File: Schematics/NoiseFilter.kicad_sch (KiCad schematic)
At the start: 97 parts, among them J68 Conn_01x04, J69 Conn_01x05, Q10 2N3906, Q11 2N3906, Q12 2N3906, Q9 2N3906, U111 TL074, U112 TL074, U113 TL074, U114 LM13700, U115 LM13700, U116 ADG409

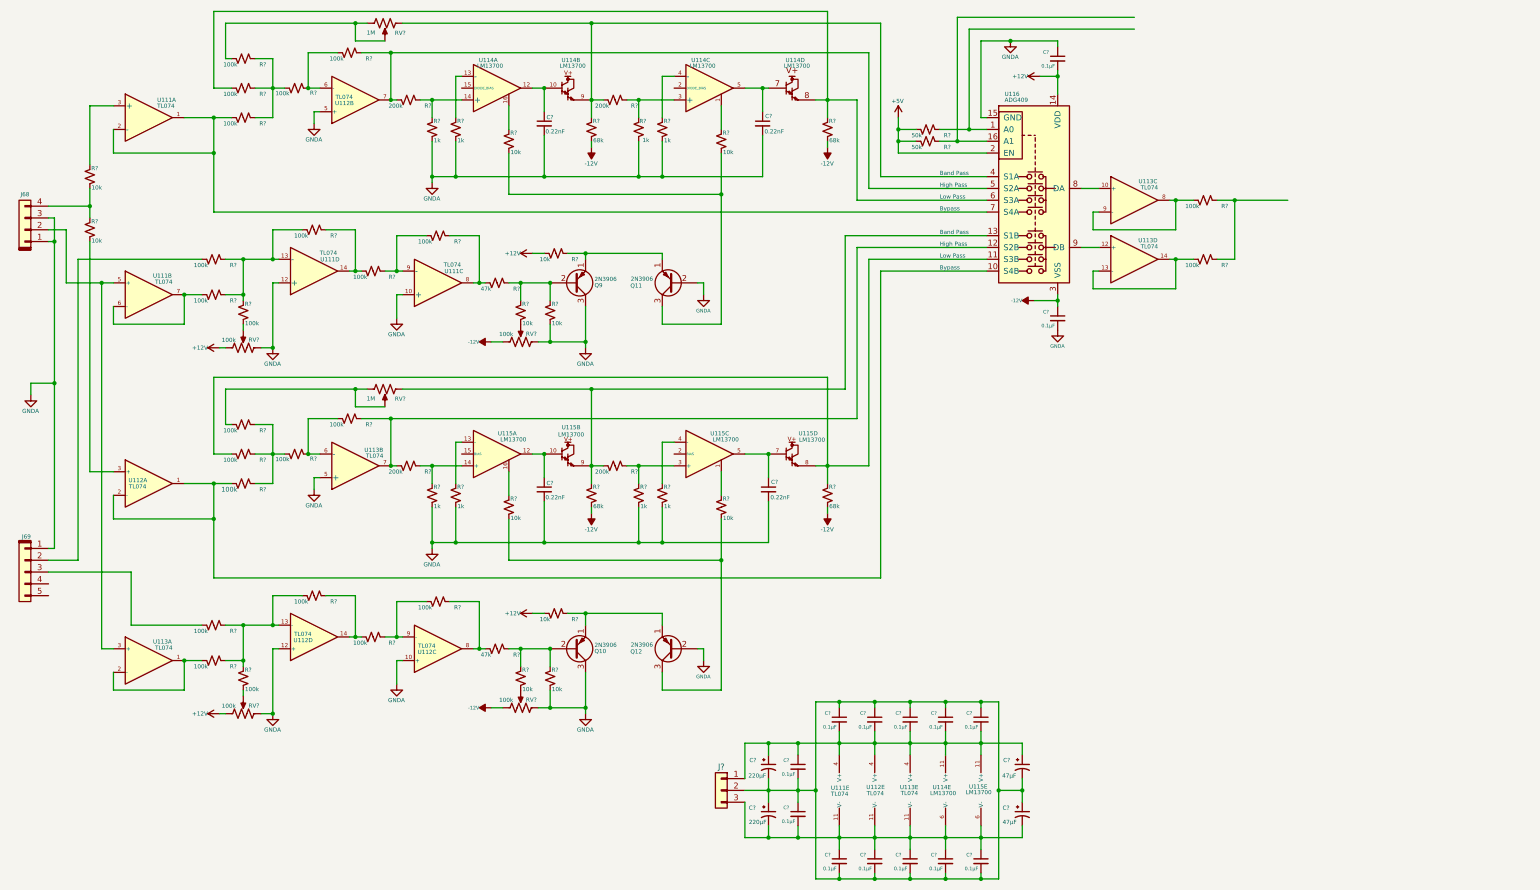
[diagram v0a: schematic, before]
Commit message: Noise boards added.
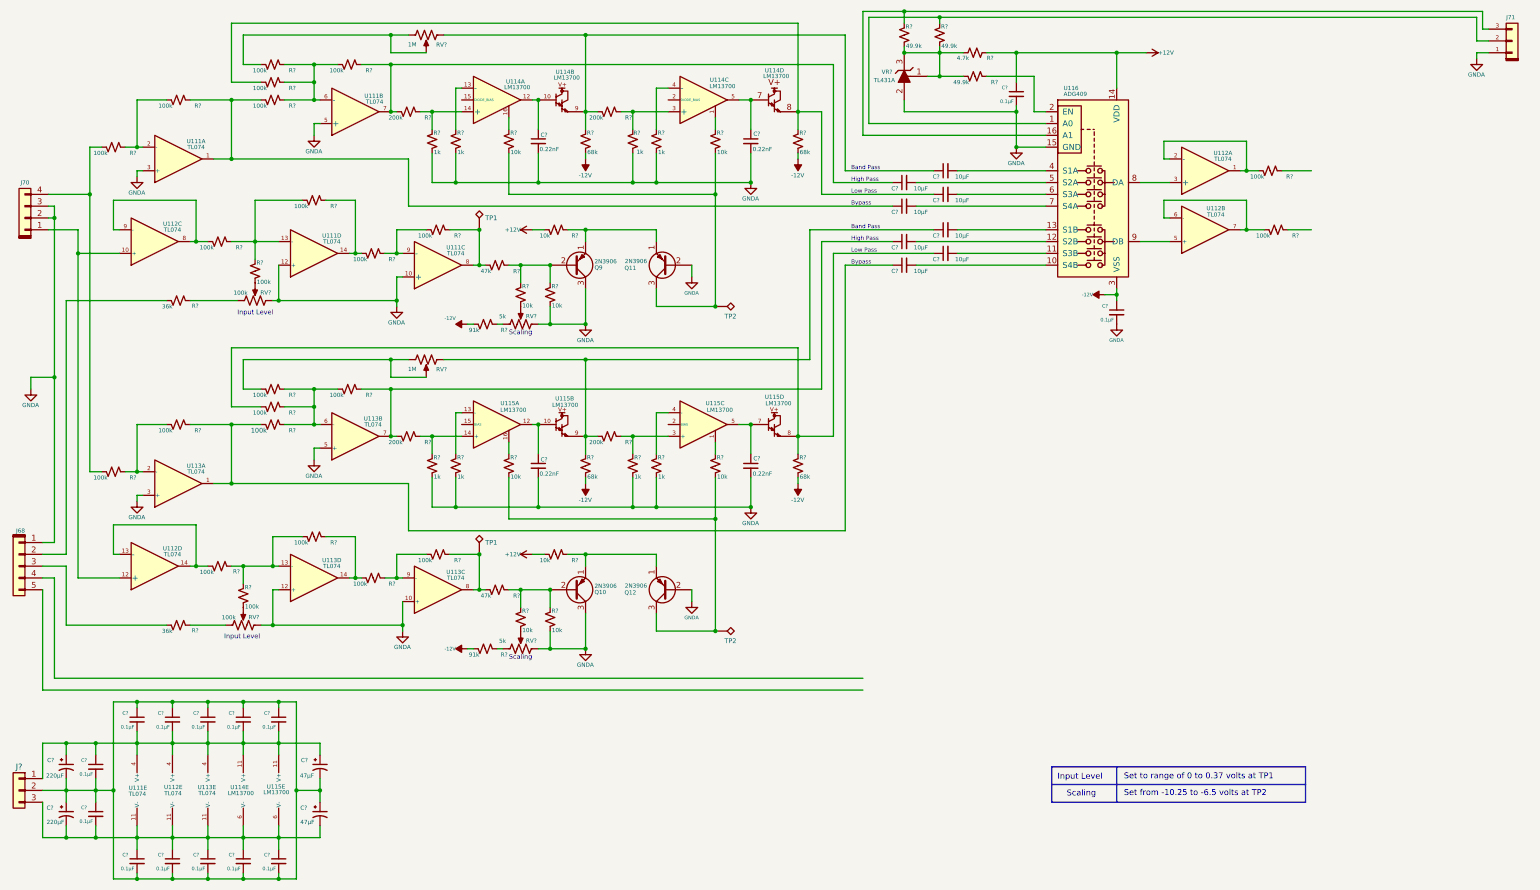
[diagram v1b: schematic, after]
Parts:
- removed R? (x2): 10k, symbol Device:R_Small_US
- removed R? (x5): 100k, symbol Device:R_Small_US
- removed R? (x2): 50k, symbol Device:R_Small_US
- removed RV?: 100k, symbol Device:R_Potentiometer_US
- added C? (x8): 10µF, symbol Device:C_Small
- added J71: Conn_01x03, symbol Connector_keyed_kicad_sym:Conn_01x03
- added R? (x5): 100k, symbol Device:R_Small_US
- added R? (x3): 49.9k, symbol Device:R_Small_US
- added R? (x2): 91k, symbol Device:R_Small_US
- added R? (x2): 36k, symbol Device:R_Small_US
- added R?: 4.7k, symbol Device:R_Small_US
- added RV?: 100k, symbol Device:R_Potentiometer_US
- added TP1, TP2: TP1, symbol Connector:TestPoint_Alt
- added TP3, TP4: TP2, symbol Connector:TestPoint_Alt
- added VR?: TL431A, digikey-footprints:TO-92-3_Formed_Leads, symbol dk_PMIC-Voltage-Reference:TL431CLPM
- RV? (x2): value 100k -> 5k
- renumbered J69 to J68, J68 to J70, U112 to U111, U113 to U111, U111 to U112, U111 to U113
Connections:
- net +12V: now also C?.1, R?.2; no longer C?.2, RV?. (3)
- net -12V: now also R?.2, R?.2; no longer RV?. (3), RV?. (3)
- net GNDA: now also C?.2, J70.2 (Pin_2), U111.3 (+), U113.10 (+), U113.12 (+), U113.3 (+), U113.5 (+), J71.1 (Pin_1), RV?. (3), VR?.2 (A); no longer C?.1, J70.1 (Pin_1), U112.10 (+), U112.12 (+), U112.5 (+)
- net at J70.4 (Pin_4): now also R?.2, R?.2
- net at R?.1, R?.2: now also U113.9 (-); no longer U112.9 (-)
- net at R?.1, R?.2: now also U113.14; no longer U111.14
- net at Q12.3 (C), R?.2, R?.2: now also TP4.1
- net at R?.1, R?.2, RV?. (3)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: now also C?.1; no longer U116.13 (S1B)
- net at R?.1, R?.2: now also U111.13 (-), R?.1; no longer U112.13 (-)
- net at J68.2 (Pin_2): now also R?.2
- net at J68.3 (Pin_3): now also R?.2
- net at U116.1 (A0): now also J71.2 (Pin_2), R?.1
- net at U116.9 (DB): now also U112.5 (+); no longer U113.12 (+)
- net at R?.1, R?.1, R?.2: now also U113.13 (-); no longer U111.13 (-)
- net at R?.1, R?.1, R?.1: now also R?.2, U113.6 (-)
- net at R?.1, R?.2: now also U113.7, C?.1; no longer U111.7, U116.12 (S2B)
- net at U111.6 (-): now also R?.1, R?.1, R?.1, R?.2; no longer R?.2
- net at R?.1, R?.2, U111.8: now also TP1.1
- net at R?.1, R?.2: now also U111.7, C?.1; no longer U112.7, U116.5 (S2A)
- net at R?.1, R?.2, RV?. (3)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: now also C?.1; no longer U116.4 (S1A)
- net at R?.1, R?.2, U114.8: now also C?.1; no longer U116.6 (S3A)
- net at Q11.3 (C), R?.2, R?.2: now also TP3.1
- net at U116.8 (DA): now also U112.3 (+); no longer U113.10 (+)
- net at U116.16 (A1): now also J71.3 (Pin_3), R?.1
- net at R?.1, R?.2: now also U113.8, TP2.1; no longer U112.8
- net at R?.1, R?.2, U115.8: now also C?.1; no longer U116.11 (S3B)
- net at U112.6 (-): now also R?.2, U112.7; no longer R?.2
- net at U112.1, U112.2 (-): now also R?.2; no longer R?.2, U116.7 (S4A)
- net at R?.1: no longer R?.1
- net at R?.1, R?.2: now also U111.14; no longer U112.14
- net +5V: no longer names the net of U116.2 (EN)
- net +5V: now also R?.1
- new net: C?.1, R?.1, R?.2, U113.1
- new net: R?.1, R?.2, U113.2 (-)
- new net: R?.2, RV?. (3)
- new net: R?.1, RV?. (3) (x4)
- new net: R?.1, R?.2, R?.2, R?.2, VR?.1 (REF), VR?.3 (K)
- new net: R?.2, U112.8, U112.9 (-)
- new net: R?.1, R?.2, U111.2 (-)
- new net: R?.2, U112.13 (-), U112.14
- new net: C?.2, U116.10 (S4B)
- new net: C?.2, U116.6 (S3A)
- new net: C?.2, U116.11 (S3B)
- new net: J70.1 (Pin_1), U112.10 (+), U112.12 (+)
- new net: C?.1, R?.1, R?.2, U111.1
- new net: C?.2, U116.12 (S2B)
- new net: C?.2, U116.13 (S1B)
- new net: C?.2, U116.4 (S1A)
- new net: C?.2, U116.5 (S2A)
- new net: C?.2, U116.7 (S4A)
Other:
- note added: "Input Level"
- note added: "Scaling"
- note added: "Set from -10.25 to -6.5 volts at TP2"
- note added: "Set to range of 0 to 0.37 volts at TP1"
- moved on the sheet: C?, J68, J70, J?, Q10, Q11, Q12, Q9, R?, RV?, U111A, U111B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

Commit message: Update with noise filter & VCA as well as envelope generator software shell.
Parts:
- removed C? (x4): 0.1µF, symbol Device:C_Small
- removed R? (x2): 100k, symbol Device:R_Small_US
- added C? (x2): 1µF, symbol Device:C_Small
- added C? (x2): 0.1µF, symbol Device:C_Small
- added C? (x2): 20pF, symbol Device:C_Small
- added D16, D17: 1N4148, Diode_THT:D_DO-35_SOD27_P7.62mm_Horizontal, symbol Diode:1N4148
- added J79: Conn_01x04, symbol Connector_keyed_kicad_sym:Conn_01x04
- added Q15, Q16: 2N3906, Package_TO_SOT_THT:TO-92_Inline, symbol Transistor_BJT:2N3906
- added R? (x4): 620, symbol Device:R_Small_US
- added R? (x7): 330k, symbol Device:R_Small_US
- added R? (x4): 1k, symbol Device:R_Small_US
- added R? (x2): 12k, symbol Device:R_Small_US
- added R? (x2): 15k, symbol Device:R_Small_US
- added R? (x2): 180k, symbol Device:R_Small_US
- added R? (x2): 33k, symbol Device:R_Small_US
- added RV? (x2): 100k, symbol Device:R_Potentiometer_US
- added unit 1 of U120
- added unit 5 of U123
- added unit 3 of U123
- added unit 2 of U123
- added unit 4 of U123
- added U124: LM13700, symbol Amplifier_Operational:LM13700
- added U125: TL072, symbol Amplifier_Operational:TL072
- renumbered J68 to J75, J70 to J77, J71 to J78, Q9 to Q11, Q10 to Q12, Q11 to Q13, Q12 to Q14, U111 to U118, U112 to U118, U112 to U119, U111 to U119, U113 to U119, U113 to U120, U112 to U120, U114 to U121, U115 to U122, U112 to U123, U116 to U126
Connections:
- net +12V: now also C?.1, C?.1, C?.1, C?.2, C?.2, C?.2, J?.1 (Pin_1), U118.4 (V+), U119.4 (V+), U120.4 (V+), U121.11 (V+), U122.11 (V+), C?.2, RV?. (3), RV?. (3), U123.4 (V+), U124.11 (V+), U125.8 (V+)
- net -12V: now also C?.1, C?.1, C?.1, C?.2, C?.2, C?.2, J?.3 (Pin_3), U118.11 (V-), U119.11 (V-), U120.11 (V-), U121.6 (V-), U122.6 (V-), C?.1, RV?. (3), RV?. (3), U123.11 (V-), U124.6 (V-), U125.4 (V-)
- net GNDA: now also C?.1, C?.1, C?.1, C?.1, C?.1, C?.1, C?.2, C?.2, C?.2, C?.2, C?.2, C?.2, J?.2 (Pin_2), C?.1, C?.2, J79.1 (Pin_1), J79.3 (Pin_3), R?.2, R?.2, R?.2, R?.2, R?.2, R?.2, U120.3 (+), U123.10 (+), U123.12 (+), U123.5 (+); no longer J77.2 (Pin_2)
- net at J75.4 (Pin_4): now also R?.2
- net at J75.5 (Pin_5): now also R?.2
- net Channel A: now reaches U123.1, U123.2 (-)
- net Channel A: now also R?.2
- net Channel B: now reaches U120.6 (-), U120.7
- net Channel B: now also R?.2
- new net: R?.1, U124.14 (+)
- new net: R?.1, R?.1, U124.13 (-)
- new net: R?.1, U124.3 (+)
- new net: C?.1, D16.1 (K), R?.1, R?.1, R?.1, R?.2, U123.9 (-)
- new net: J79.4 (Pin_4), R?.1
- new net: C?.2, R?.1, R?.2, U120.1
- new net: R?.1, U124.1
- new net: Q15.3 (C), R?.2
- new net: R?.2, RV?. (3) (x2)
- new net: R?.1, R?.1, U124.4 (-)
- new net: Q16.1 (E), R?.1, R?.1
- new net: C?.2, D17.2 (A), Q16.2 (B), U123.14
- new net: Q16.3 (C), R?.2
- new net: R?.2, U125.1, U125.2 (-)
- new net: C?.2, D16.2 (A), Q15.2 (B), U123.8
- new net: C?.1, R?.2, U123.6 (-), U124.12
- new net: R?.1, U124.16
- new net: C?.2, R?.1, R?.2, U123.7
- new net: C?.1, D17.1 (K), R?.1, R?.1, R?.2, U123.13 (-)
- new net: C?.1, R?.2, U120.2 (-), U124.5
- new net: Q15.1 (E), R?.1, R?.1
- new net: R?.2, U125.6 (-), U125.7
- new net: J79.2 (Pin_2), R?.1
- new net: R?.1, R?.2
- new net Modulation: J77.2 (Pin_2), U125.3 (+), U125.5 (+)
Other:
- note added: "OFFSET A"
- note added: "Set from -10.9 to -9.0 volts at"
- note added: "Set to range of 0 to 1.36 volts at"
- note added: "TP1"
- note added: "TP2"
- note added: "VCA in"
- note added: "to VCA"
- note removed: "Set from -10.25 to -6.5 volts at TP2"
- note removed: "Set to range of 0 to 0.37 volts at TP1"
- moved on the sheet: C?, R?, RV?, U120B, U123A, VR?

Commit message: sync up first noise board.
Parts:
- removed R? (x2): 330k, symbol Device:R_Small_US
- removed RV?: 100k, symbol Device:R_Potentiometer_US
- added R?: 330k, symbol Device:R_Small_US
- added RV?: 100k, symbol Device:R_Potentiometer_US
- C? (x2): value 1µF -> 0.1µF
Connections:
- net +12V: now also RV?. (3)
- net -12V: now also RV?. (3)
- net Mod F: now reaches J77.4 (Pin_4), R?.2, R?.2
- net Cont V: now reaches J75.4 (Pin_4), R?.2
- net Cont V: now also J75.5 (Pin_5), R?.2
- net Cont F: now reaches J75.2 (Pin_2), R?.2
- net Cont F: now also J75.3 (Pin_3), R?.2
- net at C?.1, D17.1 (K), R?.2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: now also R?.1, R?.1
- net Modulation renamed Mod V 
- net Mod V : no longer J77.2 (Pin_2)
- new net: R?.2, RV?. (3)
- new net Mod V: J77.2 (Pin_2)
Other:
- note added: "CH out"
- note added: "OFFSET"
- note removed: "OFFSET A"
- moved on the sheet: C?, D16, D17, J79, Q15, Q16, R?, RV?, U120A, U123B, U123C, U123D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

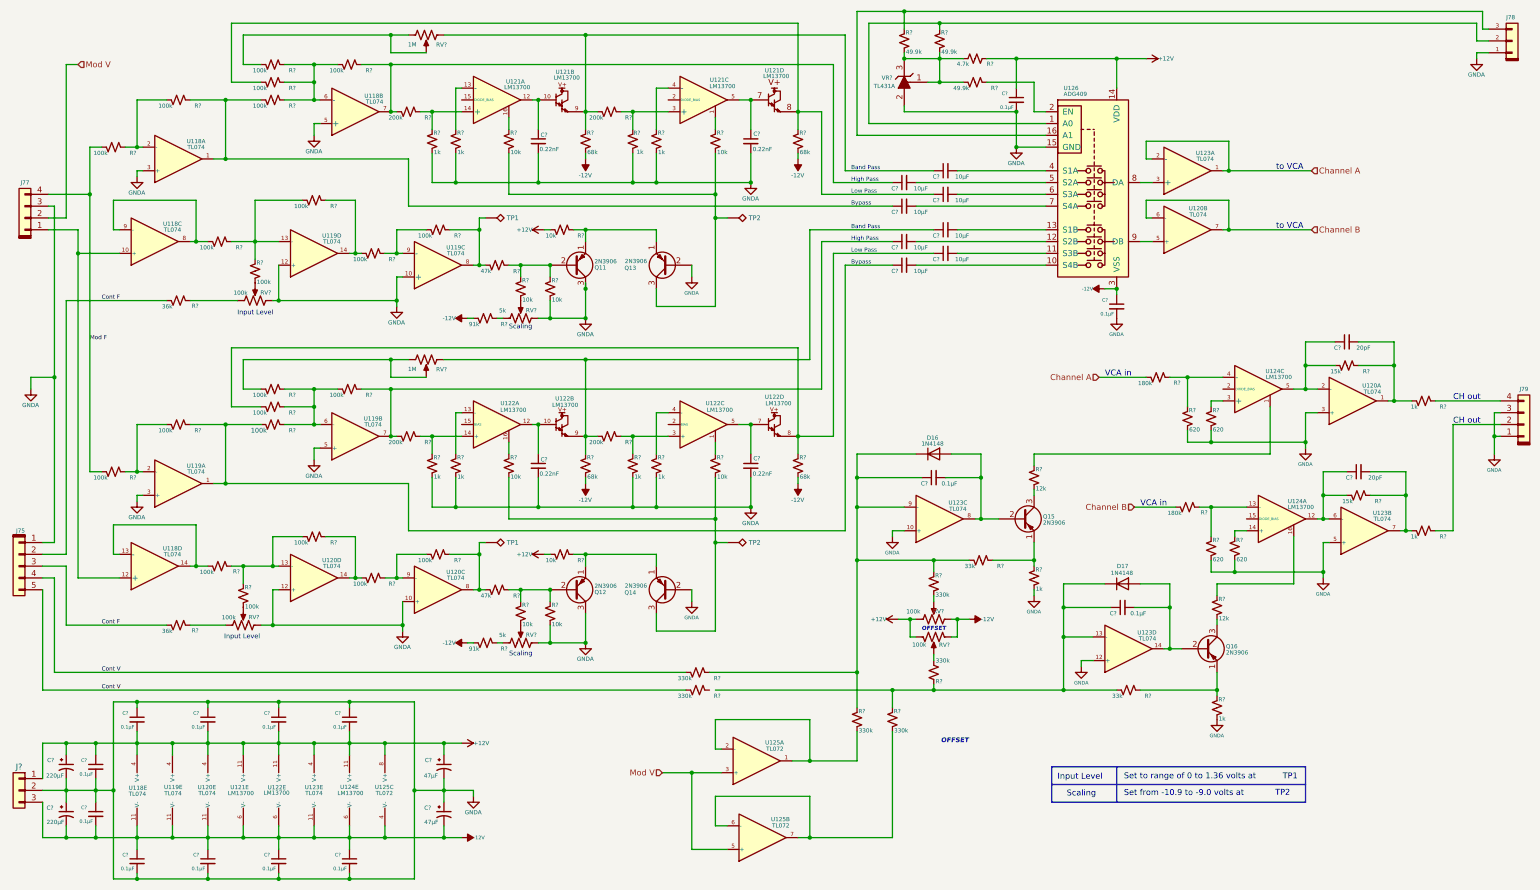
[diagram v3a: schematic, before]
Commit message: Partial software with complete hardware on best 3 state filter with 4 outputs.
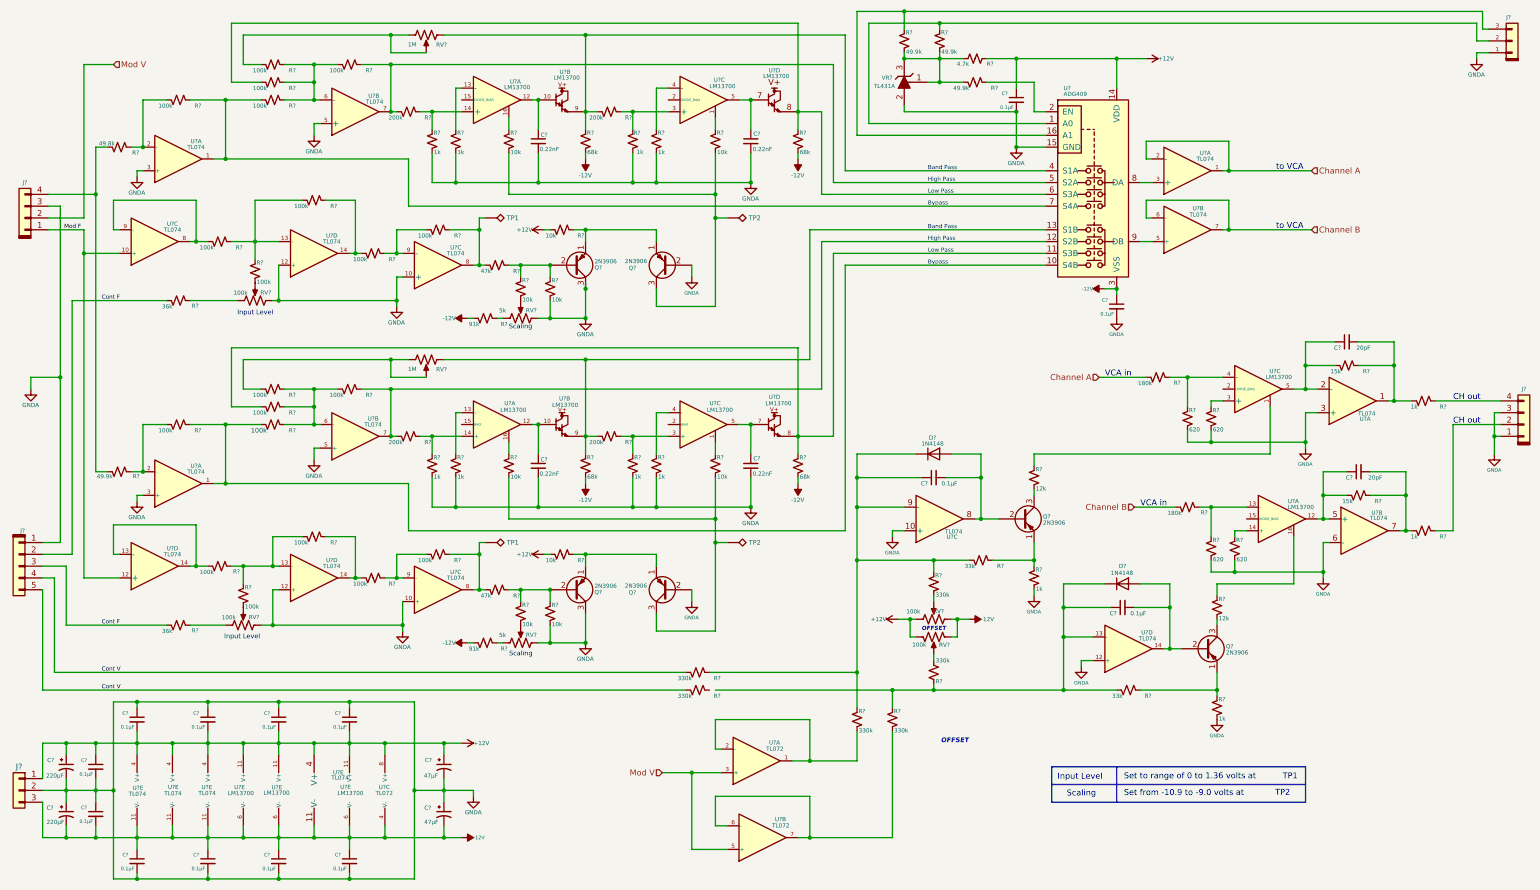
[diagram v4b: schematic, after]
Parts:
- removed C? (x8): 10µF, symbol Device:C_Small
- R?: value 100k -> 49.9k
- R?: value 100k -> 49.8k
- renumbered D16 to D?, D17 to D?, J75 to J?, J77 to J?, J79 to J?, J78 to J?, Q14 to Q?, Q16 to Q?, Q11 to Q?, Q15 to Q?, Q12 to Q?, Q13 to Q?, TP3 to TP?, TP1 to TP?, TP2 to TP?, TP4 to TP?, U123 to U?, U125 to U?, U120 to U?, U119 to U?, U124 to U?, U121 to U?, U122 to U?, U118 to U?, U126 to U?
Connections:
- net GNDA: now also U?.6 (-); no longer U?.5 (+)
- net Mod F: now also J?.1 (Pin_1), U?.10 (+), U?.12 (+); no longer J?.4 (Pin_4), R?.2, R?.2
- net at R?.1, R?.2, U?.1: now also U?.10 (S4B)
- net at R?.1, R?.2, RV?. (3)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: now also U?.13 (S1B)
- net at R?.1, R?.2, U?.7: now also U?.12 (S2B)
- net at R?.1, R?.2, U?.7: now also U?.5 (S2A)
- net at R?.1, R?.2, RV?. (3)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: now also U?.4 (S1A)
- net at C?.1, R?.2, U?.12: now also U?.5 (+); no longer U?.6 (-)
- net at R?.1, R?.2, U?.8: now also U?.6 (S3A)
- net at R?.1, R?.2, U?.8: now also U?.11 (S3B)
- net at R?.1, R?.2, U?.1: now also U?.7 (S4A)
- new net: J?.4 (Pin_4), R?.2, R?.2
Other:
- moved on the sheet: R?
